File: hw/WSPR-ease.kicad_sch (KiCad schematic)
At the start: 53 parts, among them J101 SMA, J102 SMA, J103 pwr+data, Q101 MMBF170, U101 GNSS module, U102 ESP32-S3-WROOM-1-N8R8, U103 SRV05-4, U104 TPS22918DBVR, U105 TPS74612PQWDRBRQ1, U106 LMR51430YDDCR

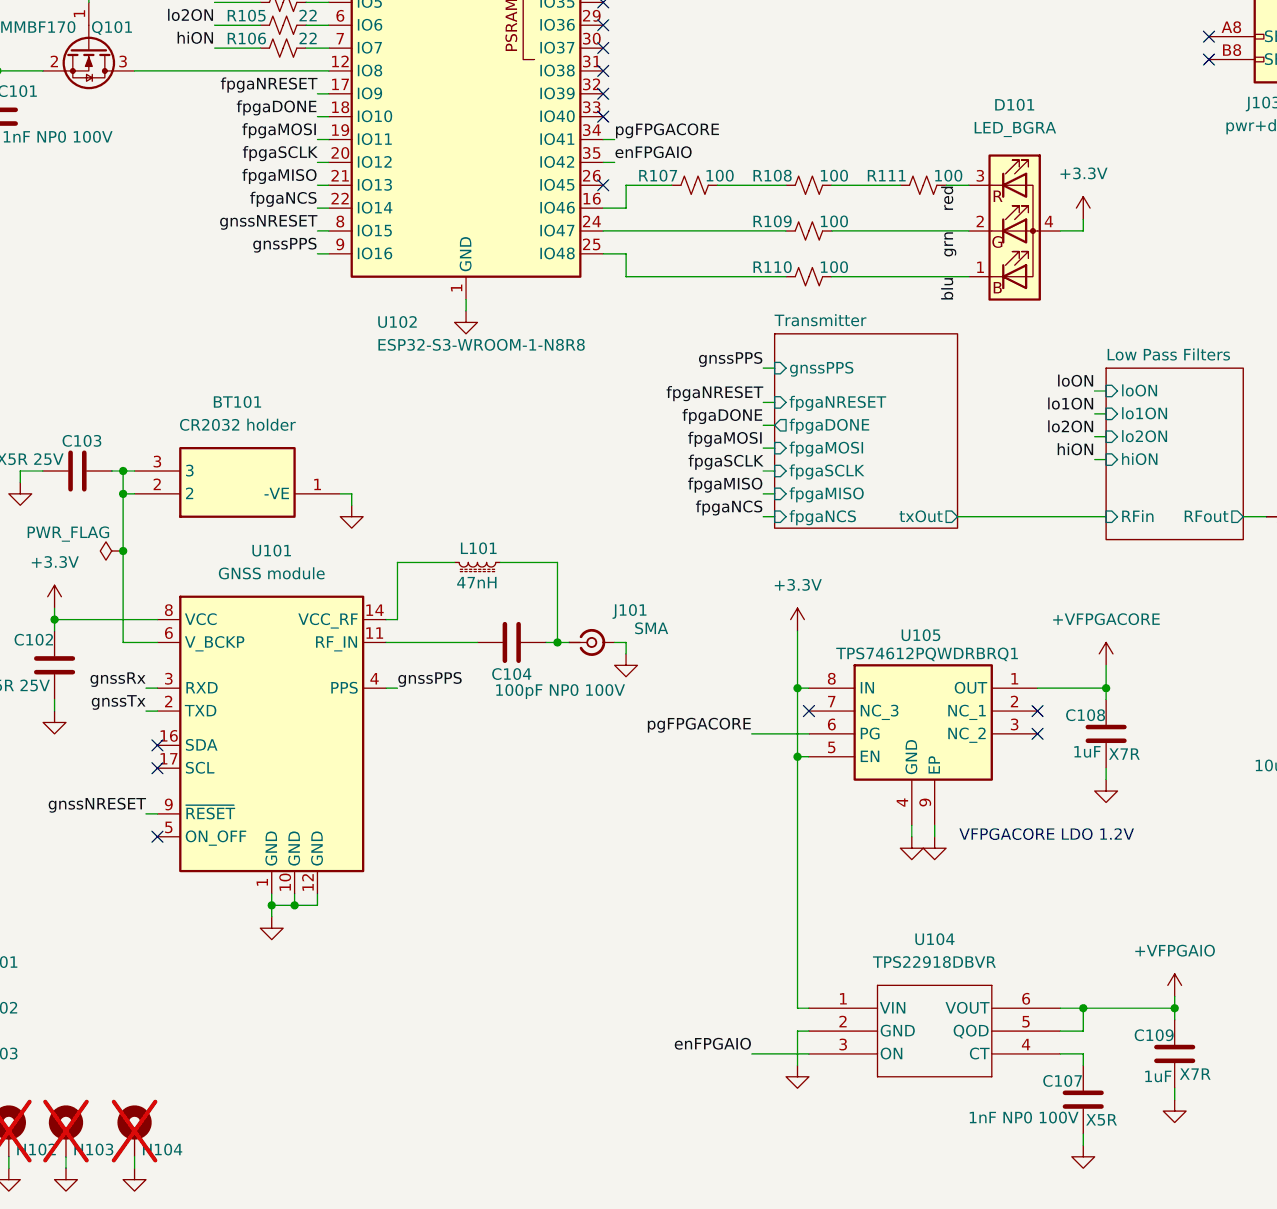
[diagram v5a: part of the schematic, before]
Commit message: Rename-o-rama to make coding style match my explicit guidelines (GEMINI ignores these for some reason). I have cleaned a few things up in the process. Code is somewhat broken right now as I prep for FPGA loading.
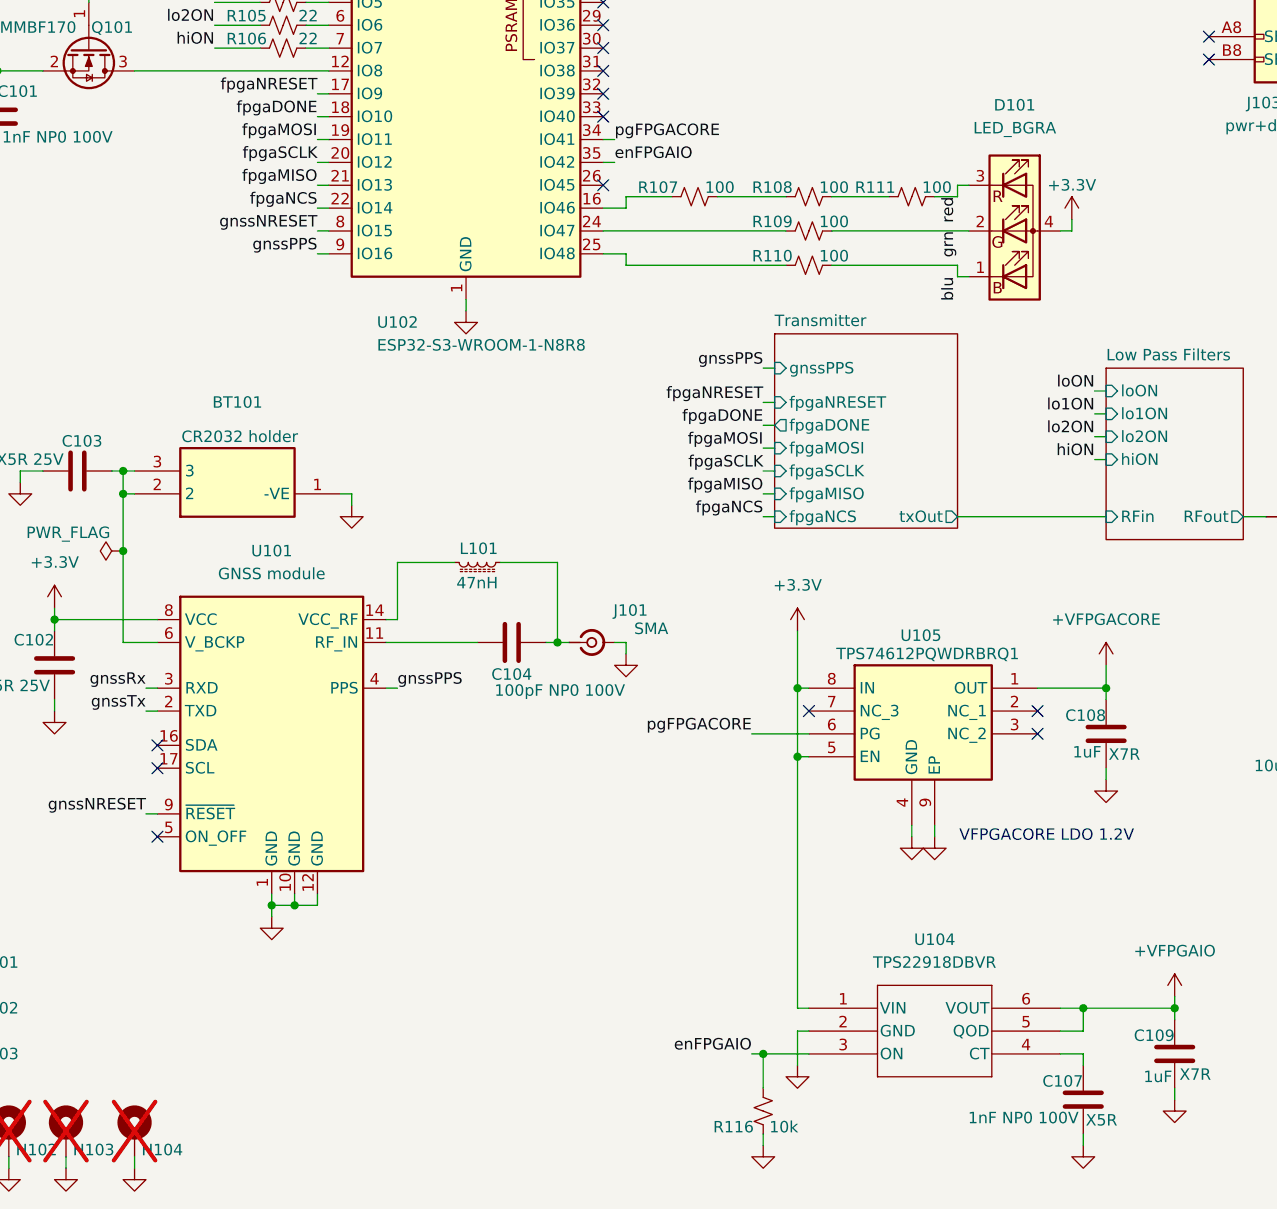
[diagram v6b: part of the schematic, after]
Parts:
- added R116: 10k, Resistor_SMD:R_0402_1005Metric, symbol Device:R_Small_US
- BT101: label (none) -> CR2032 holder
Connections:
- net GND: now also R116.1
- net enFPGAIO: now also R116.2
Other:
- moved on the sheet: R107, R108, R110, R111

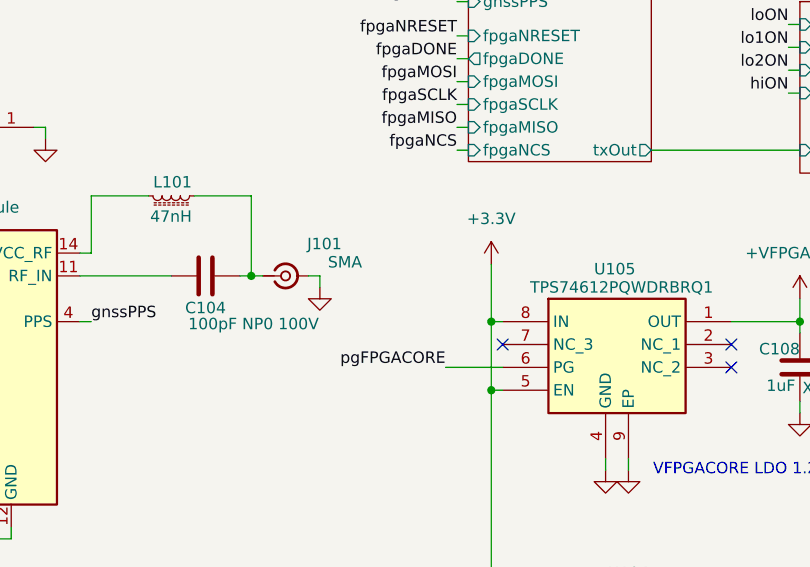
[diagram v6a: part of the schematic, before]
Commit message: Add 10k pullup to +3.3V for PG on FPGA CORE rail so we can read it from ESP32.
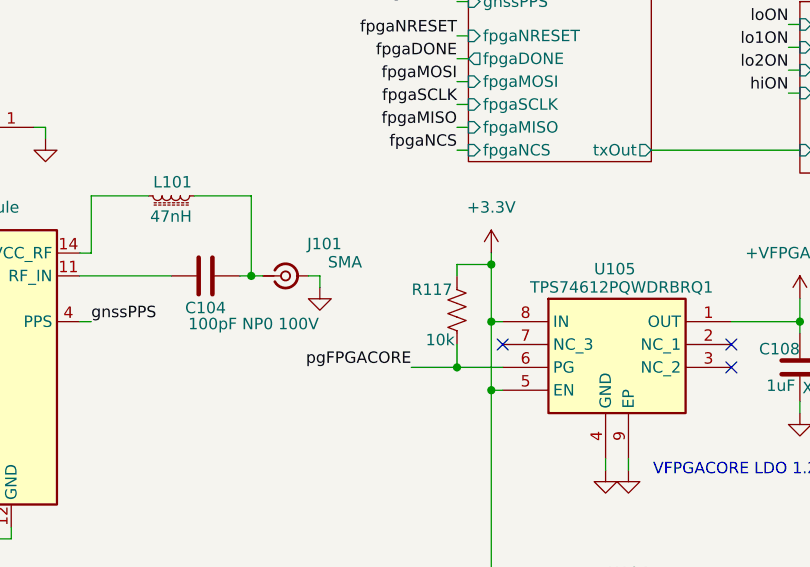
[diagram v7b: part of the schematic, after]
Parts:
- added R117: 10k, Resistor_SMD:R_0402_1005Metric, symbol Device:R_US
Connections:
- net +3.3V: now also R117.2
- net pgFPGACORE: now also R117.1

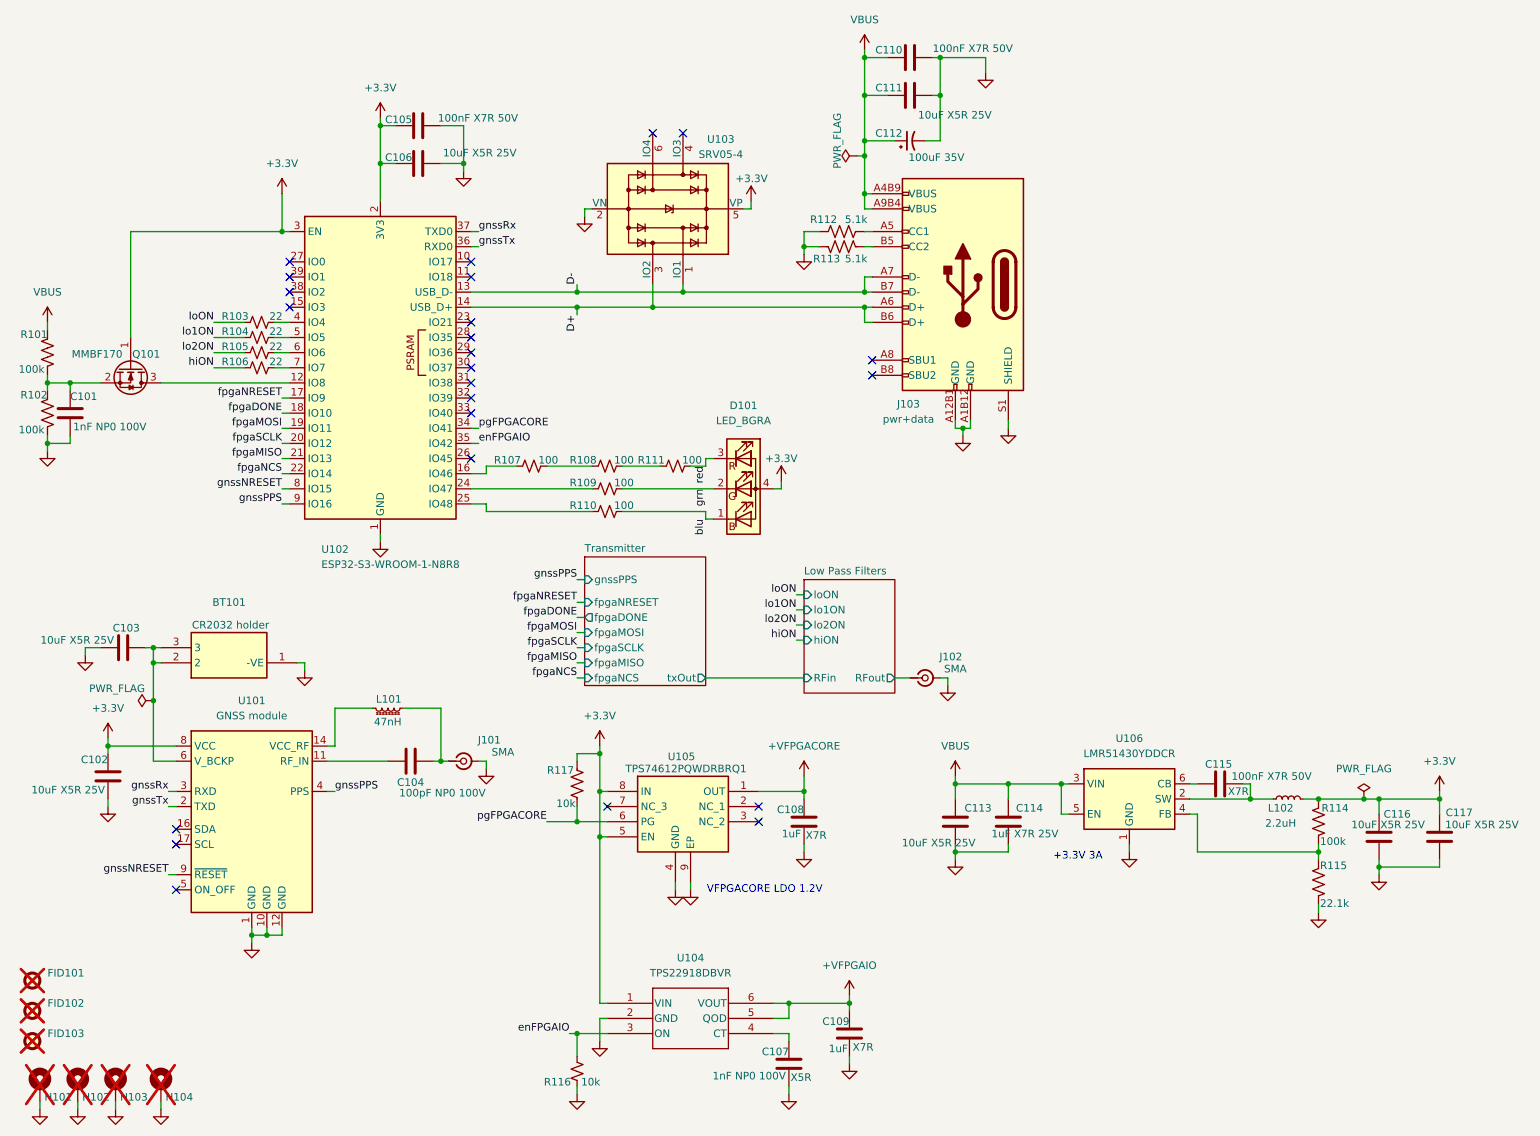
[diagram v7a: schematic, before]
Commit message: Separate FPGA config CRESET from software NRESET, add RGB heartbeat to FPGA.
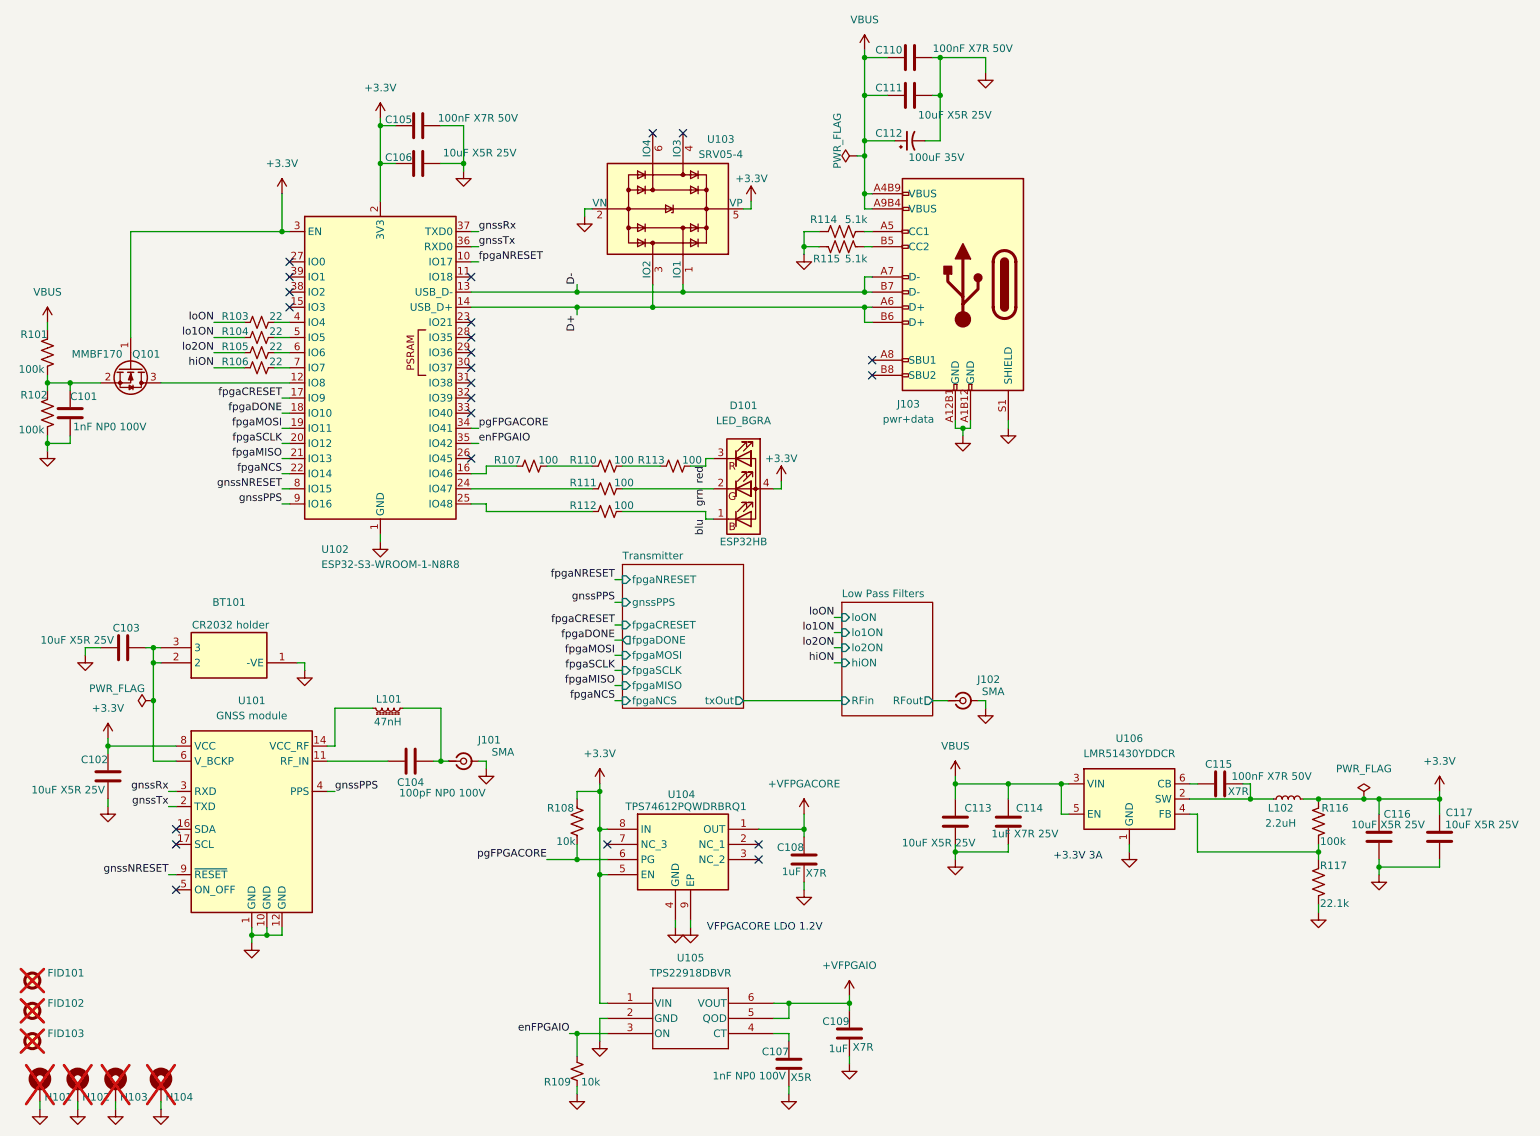
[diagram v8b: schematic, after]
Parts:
- D101: label (none) -> ESP32HB
- renumbered R117 to R108, R116 to R109, R108 to R110, R109 to R111, R110 to R112, R111 to R113, R112 to R114, R113 to R115, R114 to R116, R115 to R117, U105 to U104, U104 to U105
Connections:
- net fpgaNRESET: now also U102.10 (IO17); no longer U102.17 (IO9)
- new net fpgaCRESET: U102.17 (IO9)
- no-connect marks 24 -> 23
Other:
- sheet Transmitter ports: added fpgaCRESET; removed none
- moved on the sheet: C108, J102, R108, U104
